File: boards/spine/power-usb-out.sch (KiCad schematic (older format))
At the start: 10 parts, among them CON7 USB-A, U10 SiP32408

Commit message: BOM cleanup
Especially fix the confusing and mostly incorrect Mfg/Mfr stuff that I inherited from somewhere.
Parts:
- C62: Mfg1 (none) -> Murata; Mfg1Id (none) -> GRM219R61H105KA73D; MfgId GRM219R61H105KA73D -> (none); MfrId Murata -> (none)
- C63, C64: Mfg1 (none) -> Murata; Mfg1Id (none) -> GRM21BR71H104MA01L; MfgId GRM21BR71H104MA01L -> (none); MfrId Murata -> (none)
- CON7: Mfg1 (none) -> On-Shore Tech; Mfg1Id (none) -> USB-A1SSW6; MfgId USB-A1SSW6 -> (none); MfrId On-Shore Tech -> (none)
- F1: Mfg1 (none) -> Bel Fuse; Mfg1Id (none) -> 0ZCG0200FF2C; MfgId 0ZCG0200FF2C -> (none); MfrId Bel Fuse -> (none)
- FB5, FB6: Mfg1 (none) -> Samsung; Mfg1Id (none) -> CIS21P300NE; MfgId CIS21P300NE -> (none); MfrId Samsung -> (none)
- R29, R30: Mfg1 (none) -> Stackpole; Mfg1Id (none) -> RMCF0805JT100K; MfgId RMCF0805JT100K -> (none); MfrId Stackpole -> (none)
- U10: Mfg1 (none) -> Vishay; Mfg1Id (none) -> SIP32408DNP-T1-GE4; MfgId Vishay -> (none); MfrId SIP32408DNP-T1-GE4 -> (none)
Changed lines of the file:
@@
 F 4 "Digikey" H 5600 4050 60  0001 C CNN "Vend1"
 F 5 "SIP32408DNP-T1-GE4CT-ND" H 5600 4050 60  0001 C CNN "Vend1Id"
-F 6 "Vishay" H 5600 4050 60  0001 C CNN "MfgId"
-F 7 "SIP32408DNP-T1-GE4" H 5600 4050 60  0001 C CNN "MfrId"
+F 6 "Vishay" H 5600 4050 60  0001 C CNN "Mfg1"
+F 7 "SIP32408DNP-T1-GE4" H 5600 4050 60  0001 C CNN "Mfg1Id"
 F 8 "0.175" H 5600 4050 60  0001 C CNN "RefPrice1k"
 	1    5600 4050
@@
 F 3 "https://www.seielect.com/Catalog/SEI-RMCF_RMCP.pdf" H 4800 4550 30  0001 C CNN
 F 4 "Digikey" V 4800 4550 60  0001 C CNN "Vend1"
-F 5 "Stackpole" V 4800 4550 60  0001 C CNN "MfrId"
-F 6 "RMCF0805JT100K" V 4800 4550 60  0001 C CNN "MfgId"
+F 5 "Stackpole" V 4800 4550 60  0001 C CNN "Mfg1"
+F 6 "RMCF0805JT100K" V 4800 4550 60  0001 C CNN "Mfg1Id"
 F 7 "RMCF0805JT100KCT-ND" V 4800 4550 60  0001 C CNN "Vend1Id"
 F 8 "0.00320" V 4800 4550 60  0001 C CNN "RefPrice1k"
@@
 F 5 "Digikey" H 8000 4200 60  0001 C CNN "Vend1"
 F 6 "ED2991-ND" H 8000 4200 60  0001 C CNN "Vend1Id"
-F 7 "On-Shore Tech" H 8000 4200 60  0001 C CNN "MfrId"
-F 8 "USB-A1SSW6" H 8000 4200 60  0001 C CNN "MfgId"
+F 7 "On-Shore Tech" H 8000 4200 60  0001 C CNN "Mfg1"
+F 8 "USB-A1SSW6" H 8000 4200 60  0001 C CNN "Mfg1Id"
 	1    8000 4200
 	0    1    1    0
@@
 F 3 "http://www.samsungsem.com/kr/front/downloadcms.do?path=/kr/support/product-search/bead/__icsFiles/afieldfile/2014/11/13&fileName=S_CIS21J121NE.pdf" H 7325 4000 60  0001 C CNN
 F 4 "0.02383" H 7300 4000 60  0001 C CNN "RefPrice1k"
-F 5 "Samsung" H 7300 4000 60  0001 C CNN "MfrId"
-F 6 "CIS21P300NE" H 7300 4000 60  0001 C CNN "MfgId"
+F 5 "Samsung" H 7300 4000 60  0001 C CNN "Mfg1"
+F 6 "CIS21P300NE" H 7300 4000 60  0001 C CNN "Mfg1Id"
 F 7 "Digikey" H 7300 4000 60  0001 C CNN "Vend1"
 F 8 "1276-6370-1-ND" H 7300 4000 60  0001 C CNN "Vend1Id"
@@
 F 5 "490-9672-2-ND" V 6350 4300 60  0001 C CNN "Vend1Id"
 F 6 "Digikey" V 6350 4300 60  0001 C CNN "Vend1"
-F 7 "Murata" V 6350 4300 60  0001 C CNN "MfrId"
-F 8 "GRM21BR71H104MA01L" V 6350 4300 60  0001 C CNN "MfgId"
+F 7 "Murata" V 6350 4300 60  0001 C CNN "Mfg1"
+F 8 "GRM21BR71H104MA01L" V 6350 4300 60  0001 C CNN "Mfg1Id"
 	1    6350 4300
 	-1   0    0    1
@@
 F 3 "https://www.seielect.com/Catalog/SEI-RMCF_RMCP.pdf" H 6600 4300 30  0001 C CNN
 F 4 "Digikey" V 6600 4300 60  0001 C CNN "Vend1"
-F 5 "Stackpole" V 6600 4300 60  0001 C CNN "MfrId"
-F 6 "RMCF0805JT100K" V 6600 4300 60  0001 C CNN "MfgId"
+F 5 "Stackpole" V 6600 4300 60  0001 C CNN "Mfg1"
+F 6 "RMCF0805JT100K" V 6600 4300 60  0001 C CNN "Mfg1Id"
 F 7 "RMCF0805JT100KCT-ND" V 6600 4300 60  0001 C CNN "Vend1Id"
 F 8 "0.00320" V 6600 4300 60  0001 C CNN "RefPrice1k"
@@
 F 3 "http://www.samsungsem.com/kr/front/downloadcms.do?path=/kr/support/product-search/bead/__icsFiles/afieldfile/2014/11/13&fileName=S_CIS21J121NE.pdf" H 7325 4650 60  0001 C CNN
 F 4 "0.02383" H 7300 4650 60  0001 C CNN "RefPrice1k"
-F 5 "Samsung" H 7300 4650 60  0001 C CNN "MfrId"
-F 6 "CIS21P300NE" H 7300 4650 60  0001 C CNN "MfgId"
+F 5 "Samsung" H 7300 4650 60  0001 C CNN "Mfg1"
+F 6 "CIS21P300NE" H 7300 4650 60  0001 C CNN "Mfg1Id"
 F 7 "Digikey" H 7300 4650 60  0001 C CNN "Vend1"
 F 8 "1276-6370-1-ND" H 7300 4650 60  0001 C CNN "Vend1Id"
@@
 F 2 "Capacitors_SMD:C_0805" H 5088 4450 30  0001 C CNN
 F 3 "http://www.murata.com/~/media/webrenewal/support/library/catalog/products/capacitor/mlcc/c02e.ashx" H 5050 4600 60  0001 C CNN
-F 4 "GRM219R61H105KA73D" H 5100 4400 39  0001 L BNN "MfgId"
-F 5 "Murata" H 5050 4600 60  0001 C CNN "MfrId"
+F 4 "GRM219R61H105KA73D" H 5100 4400 39  0001 L BNN "Mfg1Id"
+F 5 "Murata" H 5050 4600 60  0001 C CNN "Mfg1"
 F 6 "Digikey" H 5050 4600 60  0001 C CNN "Vend1"
 F 7 "490-10743-2-ND" H 5050 4600 60  0001 C CNN "Vend1Id"
@@
 F 4 "Digikey" H 6900 4000 60  0001 C CNN "Vend1"
 F 5 "507-1777-1-ND" H 6900 4000 60  0001 C CNN "Vend1Id"
-F 6 "Bel Fuse" H 6900 4000 60  0001 C CNN "MfrId"
-F 7 "0ZCG0200FF2C" H 6900 4000 60  0001 C CNN "MfgId"
+F 6 "Bel Fuse" H 6900 4000 60  0001 C CNN "Mfg1"
+F 7 "0ZCG0200FF2C" H 6900 4000 60  0001 C CNN "Mfg1Id"
 F 8 "0.09403" H 6900 4000 60  0001 C CNN "RefPrice1k"
 	1    6900 4000
@@
 F 5 "490-9672-2-ND" V 7200 4300 60  0001 C CNN "Vend1Id"
 F 6 "Digikey" V 7200 4300 60  0001 C CNN "Vend1"
-F 7 "Murata" V 7200 4300 60  0001 C CNN "MfrId"
-F 8 "GRM21BR71H104MA01L" V 7200 4300 60  0001 C CNN "MfgId"
+F 7 "Murata" V 7200 4300 60  0001 C CNN "Mfg1"
+F 8 "GRM21BR71H104MA01L" V 7200 4300 60  0001 C CNN "Mfg1Id"
 	1    7200 4300
 	-1   0    0    1
@@
 72 0F 1C A9 DC 70 49 CB 79 33 88 85 99 AD 01 6C 4B 10 FC 3B 13 DE 3B 37 68 79 AD 07 BC 00 3C 0E
 3C 31 EE E3 D8 E7 0F 03 D7 7B 9F FB C1 E1 FF 01 18 C4 96 1D B8 0E 40 07 00 00 00 00 49 45 4E 44
-AE 42 60 82 00
+AE 42 60 82 F9
 EndData
 $EndBitmap

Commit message: Capacitor upgrades, BOM tidying
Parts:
- renumbered C62 to C63, C63 to C64, C64 to C65, CON7 to CON3, F1 to F2, R29 to R31, R30 to R32, U10 to U9
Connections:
- net 5V_IN: now also R31.1
- net ENABLE: now also R31.2; no longer R31.1
- net GND: no longer R31.2
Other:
- moved on the sheet: R31
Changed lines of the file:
@@
 $EndDescr
 $Comp
-L SiP32408 U10
+L SiP32408 U9
 U 1 1 564D3370
 P 5600 4050
-F 0 "U10" H 5350 4350 60  0000 L CNN
+F 0 "U9" H 5350 4350 60  0000 L CNN
 F 1 "SiP32408" H 5350 4250 60  0000 L CNN
 F 2 "TDFN4:TDFN4" H 5650 4250 60  0001 C CNN
@@
 $EndComp
 $Comp
-L R R29
+L R R31
 U 1 1 564D3371
-P 4800 4550
-F 0 "R29" V 4880 4550 50  0000 C CNN
-F 1 "100k" V 4800 4550 50  0000 C CNN
-F 2 "Resistors_SMD:R_0805" V 4730 4550 30  0001 C CNN
-F 3 "https://www.seielect.com/Catalog/SEI-RMCF_RMCP.pdf" H 4800 4550 30  0001 C CNN
-F 4 "Digikey" V 4800 4550 60  0001 C CNN "Vend1"
-F 5 "Stackpole" V 4800 4550 60  0001 C CNN "Mfg1"
-F 6 "RMCF0805JT100K" V 4800 4550 60  0001 C CNN "Mfg1Id"
-F 7 "RMCF0805JT100KCT-ND" V 4800 4550 60  0001 C CNN "Vend1Id"
-F 8 "0.00320" V 4800 4550 60  0001 C CNN "RefPrice1k"
-	1    4800 4550
-	1    0    0    -1
+P 4600 4150
+F 0 "R31" V 4680 4150 50  0000 C CNN
+F 1 "100k" V 4600 4150 50  0000 C CNN
+F 2 "Resistors_SMD:R_0805" V 4530 4150 30  0001 C CNN
+F 3 "https://www.seielect.com/Catalog/SEI-RMCF_RMCP.pdf" H 4600 4150 30  0001 C CNN
+F 4 "Digikey" V 4600 4150 60  0001 C CNN "Vend1"
+F 5 "Stackpole" V 4600 4150 60  0001 C CNN "Mfg1"
+F 6 "RMCF0805JT100K" V 4600 4150 60  0001 C CNN "Mfg1Id"
+F 7 "RMCF0805JT100KCT-ND" V 4600 4150 60  0001 C CNN "Vend1Id"
+F 8 "0.00320" V 4600 4150 60  0001 C CNN "RefPrice1k"
+	1    4600 4150
+	0    1    1    0
 $EndComp
 $Comp
-L GND #PWR0131
-U 1 1 564D3372
-P 4800 4750
-F 0 "#PWR0131" H 4800 4500 50  0001 C CNN
-F 1 "GND" H 4800 4600 50  0000 C CNN
-F 2 "" H 4800 4750 60  0000 C CNN
-F 3 "" H 4800 4750 60  0000 C CNN
-	1    4800 4750
-	1    0    0    -1
-$EndComp
-$Comp
-L USB_A CON7
+L USB_A CON3
 U 1 1 564D3373
 P 8000 4200
-F 0 "CON7" H 8200 4000 50  0000 C CNN
+F 0 "CON3" H 8200 4000 50  0000 C CNN
 F 1 "USB-A" H 7950 4400 50  0000 C CNN
 F 2 "Connect:USB_A_Vertical" V 7950 4100 60  0001 C CNN
@@
 $EndComp
 $Comp
-L GND #PWR0132
+L GND #PWR143
 U 1 1 564D3375
 P 6100 4750
-F 0 "#PWR0132" H 6100 4500 50  0001 C CNN
+F 0 "#PWR143" H 6100 4500 50  0001 C CNN
 F 1 "GND" H 6100 4600 50  0000 C CNN
 F 2 "" H 6100 4750 60  0000 C CNN
@@
 $EndComp
 $Comp
-L C C63
+L C C64
 U 1 1 564D3376
 P 6350 4300
-F 0 "C63" V 6400 4100 50  0000 L CNN
+F 0 "C64" V 6400 4100 50  0000 L CNN
 F 1 "0.1uF" V 6400 4400 50  0000 L CNN
 F 2 "Capacitors_SMD:C_0805" H 6388 4150 30  0001 C CNN
@@
 $EndComp
 $Comp
-L R R30
+L R R32
 U 1 1 564D3377
 P 6600 4300
-F 0 "R30" V 6680 4300 50  0000 C CNN
+F 0 "R32" V 6680 4300 50  0000 C CNN
 F 1 "100k" V 6600 4300 50  0000 C CNN
 F 2 "Resistors_SMD:R_0805" V 6530 4300 30  0001 C CNN
@@
 $EndComp
 $Comp
-L C C62
+L C C63
 U 1 1 564D3379
 P 5050 4600
-F 0 "C62" H 5100 4700 50  0000 L CNN
+F 0 "C63" H 5100 4700 50  0000 L CNN
 F 1 "1uF " H 5100 4500 50  0000 L CNN
 F 2 "Capacitors_SMD:C_0805" H 5088 4450 30  0001 C CNN
@@
 $EndComp
 $Comp
-L GND #PWR0133
+L GND #PWR142
 U 1 1 564D337A
 P 5050 4750
-F 0 "#PWR0133" H 5050 4500 50  0001 C CNN
+F 0 "#PWR142" H 5050 4500 50  0001 C CNN
 F 1 "GND" H 5050 4600 50  0000 C CNN
 F 2 "" H 5050 4750 60  0000 C CNN
@@
 $EndComp
 $Comp
-L F_Small F1
+L F_Small F2
 U 1 1 564D338C
 P 6900 4000
-F 0 "F1" H 6860 4060 50  0000 L CNN
+F 0 "F2" H 6860 4060 50  0000 L CNN
 F 1 "2A PTC" H 6780 3940 50  0000 L CNN
 F 2 "Resistors_SMD:R_1812" H 6900 4000 60  0001 C CNN
@@
 Text HLabel 3200 4000 0    60   Input ~ 0
 5V_IN
-Text HLabel 4550 4300 0    60   Input ~ 0
+Text HLabel 4100 4300 0    60   Input ~ 0
 ENABLE
 Wire Wire Line
-	4800 4750 4800 4700
-Wire Wire Line
-	4550 4300 5150 4300
-Wire Wire Line
-	4800 4400 4800 4300
-Connection ~ 4800 4300
+	4100 4300 5150 4300
 Wire Wire Line
 	7700 4100 7600 4100
@@
 Connection ~ 6600 4650
 Wire Wire Line
-	5050 4450 5050 4000
+	5050 4000 5050 4450
 Wire Wire Line
 	3200 4000 5150 4000
@@
 	6100 4650 7300 4650
 $Comp
-L C C64
+L C C65
 U 1 1 564E8130
 P 7200 4300
-F 0 "C64" V 7250 4100 50  0000 L CNN
+F 0 "C65" V 7250 4100 50  0000 L CNN
 F 1 "0.1uF" V 7250 4400 50  0000 L CNN
 F 2 "Capacitors_SMD:C_0805" H 7238 4150 30  0001 C CNN
@@
 72 0F 1C A9 DC 70 49 CB 79 33 88 85 99 AD 01 6C 4B 10 FC 3B 13 DE 3B 37 68 79 AD 07 BC 00 3C 0E
 3C 31 EE E3 D8 E7 0F 03 D7 7B 9F FB C1 E1 FF 01 18 C4 96 1D B8 0E 40 07 00 00 00 00 49 45 4E 44
-AE 42 60 82 F9
+AE 42 60 82 00
 EndData
 $EndBitmap
@@
 A
 $Comp
-L Earth #PWR0134
+L Earth #PWR144
 U 1 1 565B70B7
 P 8100 4500
-F 0 "#PWR0134" H 8100 4250 50  0001 C CNN
+F 0 "#PWR144" H 8100 4250 50  0001 C CNN
 F 1 "Earth" H 8100 4350 50  0001 C CNN
 F 2 "" H 8100 4500 60  0000 C CNN
@@
 	1    0    0    -1
 $EndComp
+Wire Wire Line
+	4450 4150 4350 4150
+Wire Wire Line
+	4350 4150 4350 4300
+Connection ~ 4350 4300
+Wire Wire Line
+	4750 4150 4850 4150
+Wire Wire Line
+	4850 4150 4850 4000
+Connection ~ 4850 4000
 $EndSCHEMATC

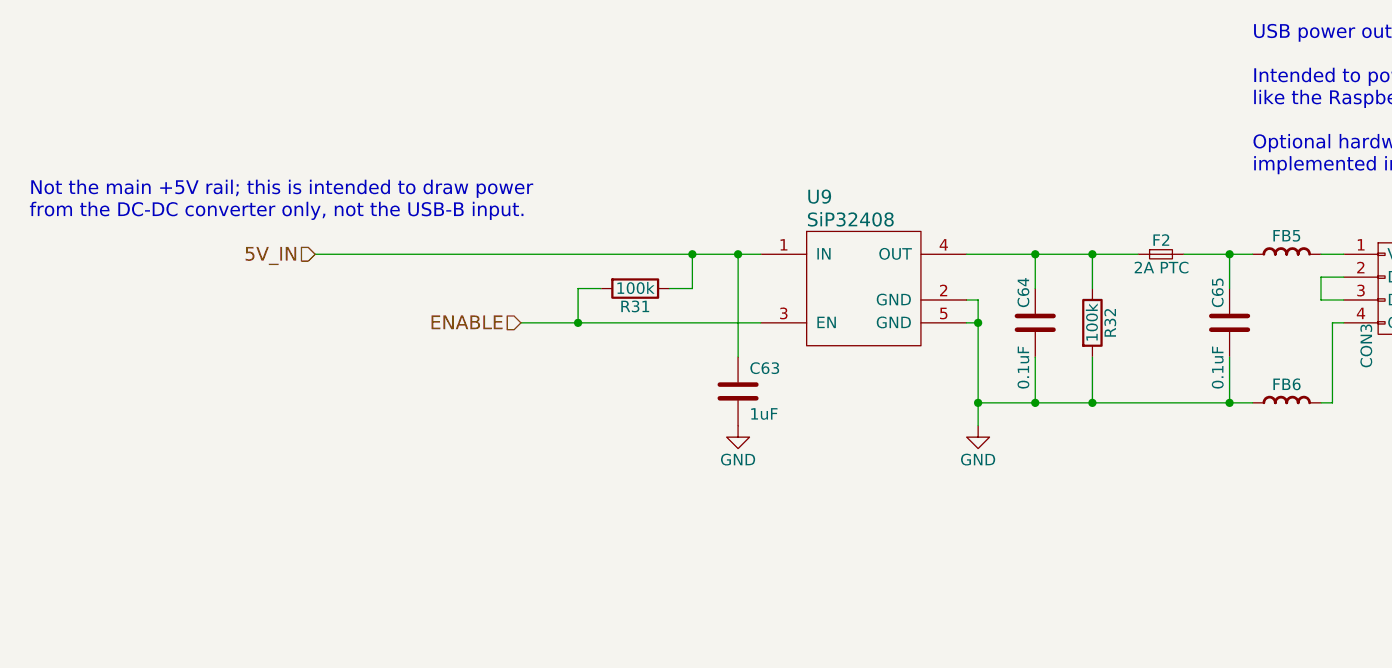
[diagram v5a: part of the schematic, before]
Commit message: Schematics stabilizing for next proto, starting PCB updates
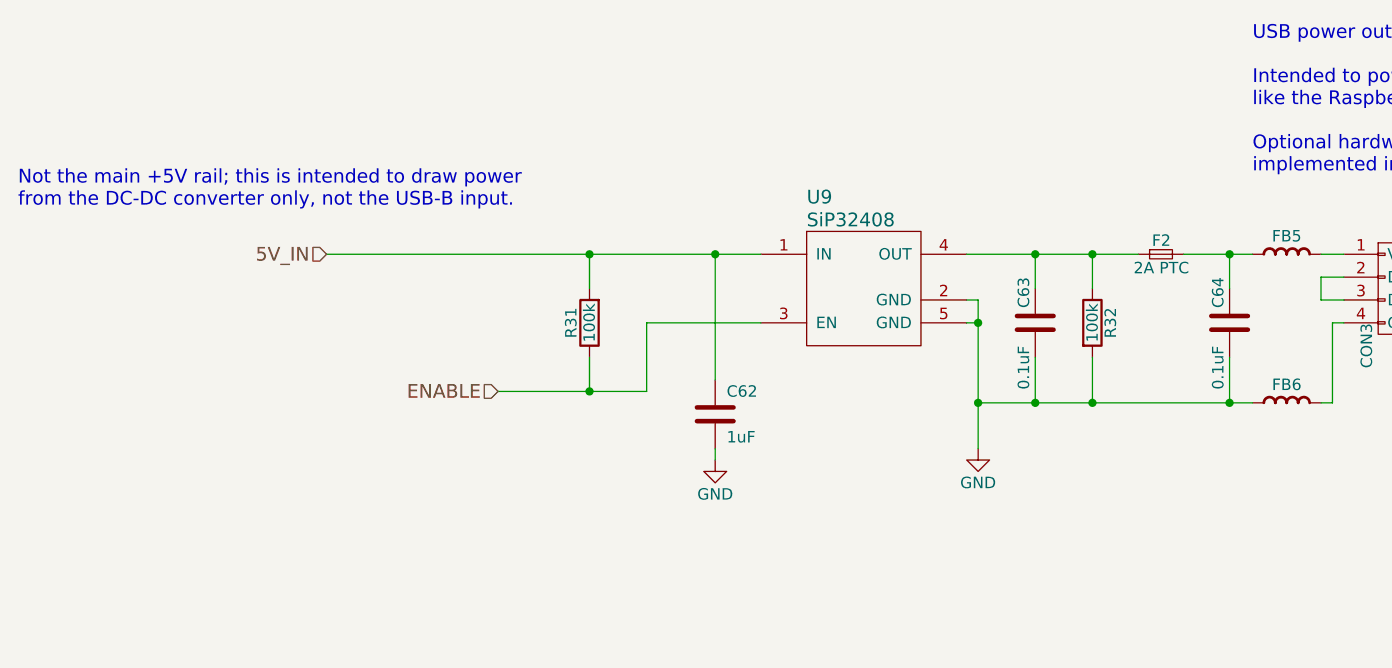
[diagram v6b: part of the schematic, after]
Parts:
- renumbered C63 to C62, C64 to C63, C65 to C64
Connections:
- net 5V_IN: now also R31.2; no longer R31.1
- net ENABLE: now also R31.1; no longer R31.2
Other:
- moved on the sheet: C62, R31
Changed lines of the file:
@@
 L R R31
 U 1 1 564D3371
-P 4600 4150
-F 0 "R31" V 4680 4150 50  0000 C CNN
-F 1 "100k" V 4600 4150 50  0000 C CNN
-F 2 "Resistors_SMD:R_0805" V 4530 4150 30  0001 C CNN
-F 3 "https://www.seielect.com/Catalog/SEI-RMCF_RMCP.pdf" H 4600 4150 30  0001 C CNN
-F 4 "Digikey" V 4600 4150 60  0001 C CNN "Vend1"
-F 5 "Stackpole" V 4600 4150 60  0001 C CNN "Mfg1"
-F 6 "RMCF0805JT100K" V 4600 4150 60  0001 C CNN "Mfg1Id"
-F 7 "RMCF0805JT100KCT-ND" V 4600 4150 60  0001 C CNN "Vend1Id"
-F 8 "0.00320" V 4600 4150 60  0001 C CNN "RefPrice1k"
-	1    4600 4150
-	0    1    1    0
+P 4400 4300
+F 0 "R31" V 4480 4300 50  0000 C CNN
+F 1 "100k" V 4400 4300 50  0000 C CNN
+F 2 "Resistors_SMD:R_0805" V 4330 4300 30  0001 C CNN
+F 3 "https://www.seielect.com/Catalog/SEI-RMCF_RMCP.pdf" H 4400 4300 30  0001 C CNN
+F 4 "Digikey" V 4400 4300 60  0001 C CNN "Vend1"
+F 5 "Stackpole" V 4400 4300 60  0001 C CNN "Mfg1"
+F 6 "RMCF0805JT100K" V 4400 4300 60  0001 C CNN "Mfg1Id"
+F 7 "RMCF0805JT100KCT-ND" V 4400 4300 60  0001 C CNN "Vend1Id"
+F 8 "0.00320" V 4400 4300 60  0001 C CNN "RefPrice1k"
+	1    4400 4300
+	-1   0    0    1
 $EndComp
 $Comp
@@
 L GND #PWR0142
 U 1 1 564D3375
-P 6100 4750
-F 0 "#PWR0142" H 6100 4500 50  0001 C CNN
-F 1 "GND" H 6100 4600 50  0000 C CNN
-F 2 "" H 6100 4750 60  0000 C CNN
-F 3 "" H 6100 4750 60  0000 C CNN
-	1    6100 4750
+P 6100 4850
+F 0 "#PWR0142" H 6100 4600 50  0001 C CNN
+F 1 "GND" H 6100 4700 50  0000 C CNN
+F 2 "" H 6100 4850 60  0000 C CNN
+F 3 "" H 6100 4850 60  0000 C CNN
+	1    6100 4850
 	1    0    0    -1
 $EndComp
 $Comp
-L C C64
+L C C63
 U 1 1 564D3376
 P 6350 4300
-F 0 "C64" V 6400 4100 50  0000 L CNN
+F 0 "C63" V 6400 4100 50  0000 L CNN
 F 1 "0.1uF" V 6400 4400 50  0000 L CNN
 F 2 "Capacitors_SMD:C_0805" H 6388 4150 30  0001 C CNN
@@
 $EndComp
 $Comp
-L C C63
+L C C62
 U 1 1 564D3379
-P 5050 4600
-F 0 "C63" H 5100 4700 50  0000 L CNN
-F 1 "1uF " H 5100 4500 50  0000 L CNN
-F 2 "Capacitors_SMD:C_0805" H 5088 4450 30  0001 C CNN
-F 3 "http://www.murata.com/~/media/webrenewal/support/library/catalog/products/capacitor/mlcc/c02e.ashx" H 5050 4600 60  0001 C CNN
-F 4 "GRM219R61H105KA73D" H 5100 4400 39  0001 L BNN "Mfg1Id"
-F 5 "Murata" H 5050 4600 60  0001 C CNN "Mfg1"
-F 6 "Digikey" H 5050 4600 60  0001 C CNN "Vend1"
-F 7 "490-10743-2-ND" H 5050 4600 60  0001 C CNN "Vend1Id"
-F 8 "0.03980" H 5050 4600 60  0001 C CNN "RefPrice1k"
-	1    5050 4600
+P 4950 4700
+F 0 "C62" H 5000 4800 50  0000 L CNN
+F 1 "1uF " H 5000 4600 50  0000 L CNN
+F 2 "Capacitors_SMD:C_0805" H 4988 4550 30  0001 C CNN
+F 3 "http://www.murata.com/~/media/webrenewal/support/library/catalog/products/capacitor/mlcc/c02e.ashx" H 4950 4700 60  0001 C CNN
+F 4 "GRM219R61H105KA73D" H 5000 4500 39  0001 L BNN "Mfg1Id"
+F 5 "Murata" H 4950 4700 60  0001 C CNN "Mfg1"
+F 6 "Digikey" H 4950 4700 60  0001 C CNN "Vend1"
+F 7 "490-10743-2-ND" H 4950 4700 60  0001 C CNN "Vend1Id"
+F 8 "0.03980" H 4950 4700 60  0001 C CNN "RefPrice1k"
+	1    4950 4700
 	1    0    0    -1
 $EndComp
@@
 L GND #PWR0143
 U 1 1 564D337A
-P 5050 4750
-F 0 "#PWR0143" H 5050 4500 50  0001 C CNN
-F 1 "GND" H 5050 4600 50  0000 C CNN
-F 2 "" H 5050 4750 60  0000 C CNN
-F 3 "" H 5050 4750 60  0000 C CNN
-	1    5050 4750
+P 4950 4900
+F 0 "#PWR0143" H 4950 4650 50  0001 C CNN
+F 1 "GND" H 4950 4750 50  0000 C CNN
+F 2 "" H 4950 4900 60  0000 C CNN
+F 3 "" H 4950 4900 60  0000 C CNN
+	1    4950 4900
 	1    0    0    -1
 $EndComp
@@
 	1    0    0    -1
 $EndComp
-Text HLabel 3200 4000 0    60   Input ~ 0
+Text HLabel 3250 4000 0    60   Input ~ 0
 5V_IN
-Text HLabel 4100 4300 0    60   Input ~ 0
+Text HLabel 4000 4600 0    60   Input ~ 0
 ENABLE
 Wire Wire Line
-	4100 4300 5150 4300
-Wire Wire Line
 	7700 4100 7600 4100
 Wire Wire Line
@@
 	6050 4300 6100 4300
 Wire Wire Line
-	6100 4200 6100 4750
+	6100 4200 6100 4850
 Wire Wire Line
 	6050 4200 6100 4200
@@
 Connection ~ 6600 4650
 Wire Wire Line
-	5050 4000 5050 4450
-Wire Wire Line
-	3200 4000 5150 4000
+	4950 4000 4950 4550
+Wire Wire Line
+	3250 4000 5150 4000
 Wire Wire Line
 	7000 4000 7300 4000
-Connection ~ 5050 4000
+Connection ~ 4950 4000
 Wire Wire Line
 	7600 4650 7650 4650
@@
 	6100 4650 7300 4650
 $Comp
-L C C65
+L C C64
 U 1 1 564E8130
 P 7200 4300
-F 0 "C65" V 7250 4100 50  0000 L CNN
+F 0 "C64" V 7250 4100 50  0000 L CNN
 F 1 "0.1uF" V 7250 4400 50  0000 L CNN
 F 2 "Capacitors_SMD:C_0805" H 7238 4150 30  0001 C CNN
@@
 	7200 4450 7200 4650
 Connection ~ 7200 4650
-Text Notes 1950 3850 0    60   ~ 0
+Text Notes 1900 3800 0    60   ~ 0
 Not the main +5V rail; this is intended to draw power\nfrom the DC-DC converter only, not the USB-B input.
 Text Notes 7300 3650 0    60   ~ 0
@@
 72 0F 1C A9 DC 70 49 CB 79 33 88 85 99 AD 01 6C 4B 10 FC 3B 13 DE 3B 37 68 79 AD 07 BC 00 3C 0E
 3C 31 EE E3 D8 E7 0F 03 D7 7B 9F FB C1 E1 FF 01 18 C4 96 1D B8 0E 40 07 00 00 00 00 49 45 4E 44
-AE 42 60 82 4D
+AE 42 60 82 00
 EndData
 $EndBitmap
@@
 $EndComp
 Wire Wire Line
-	4450 4150 4350 4150
-Wire Wire Line
-	4350 4150 4350 4300
-Connection ~ 4350 4300
-Wire Wire Line
-	4750 4150 4850 4150
-Wire Wire Line
-	4850 4150 4850 4000
-Connection ~ 4850 4000
+	4950 4850 4950 4900
+Wire Wire Line
+	5150 4300 4650 4300
+Wire Wire Line
+	4650 4300 4650 4600
+Wire Wire Line
+	4650 4600 4000 4600
+Wire Wire Line
+	4400 4150 4400 4000
+Connection ~ 4400 4000
+Wire Wire Line
+	4400 4450 4400 4600
+Connection ~ 4400 4600
 $EndSCHEMATC
